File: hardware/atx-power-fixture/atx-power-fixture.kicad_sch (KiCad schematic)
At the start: 32 parts, among them J1 ATX24RH, J2 Screw_Terminal_01x02, J3 BINDING_POST, J4 BINDING_POST, J5 Console FTDI, Q1 DMG2301L, Q2 2N7002, SW1 SW_SPST, SW2 SW_SPST, U1 SSD1306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

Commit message: Layout + gerbers for ATX power fixture
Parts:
- D1: footprint UltraLibrarian:355010RFT -> LED_THT:LED_D3.0mm
- J2: footprint (none) -> TerminalBlock:TerminalBlock_Altech_AK300-2_P5.00mm
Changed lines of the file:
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@@
       (effects (font (size 1.27 1.27)) (justify left))
     )
-    (property "Footprint" "" (id 2) (at 256.159 60.452 0)
+    (property "Footprint" "TerminalBlock:TerminalBlock_Altech_AK300-2_P5.00mm" (id 2) (at 256.159 60.452 0)
       (effects (font (size 1.27 1.27)) hide)
     )
@@
     (property "Reference" "D1" (id 0) (at 116.7765 103.251 0))
     (property "Value" "LED" (id 1) (at 116.7765 105.791 0))
-    (property "Footprint" "UltraLibrarian:355010RFT" (id 2) (at 115.189 110.109 0)
+    (property "Footprint" "LED_THT:LED_D3.0mm" (id 2) (at 115.189 110.109 0)
       (effects (font (size 1.27 1.27)) hide)
     )
@@
     )
     (path "/f43d542b-9e51-43f6-abab-b13ad18f0eab"
-      (reference "D1") (unit 1) (value "LED") (footprint "UltraLibrarian:355010RFT")
+      (reference "D1") (unit 1) (value "LED") (footprint "LED_THT:LED_D3.0mm")
     )
     (path "/5b49dbbc-6d9b-40fe-9cc9-73d9104b1539"

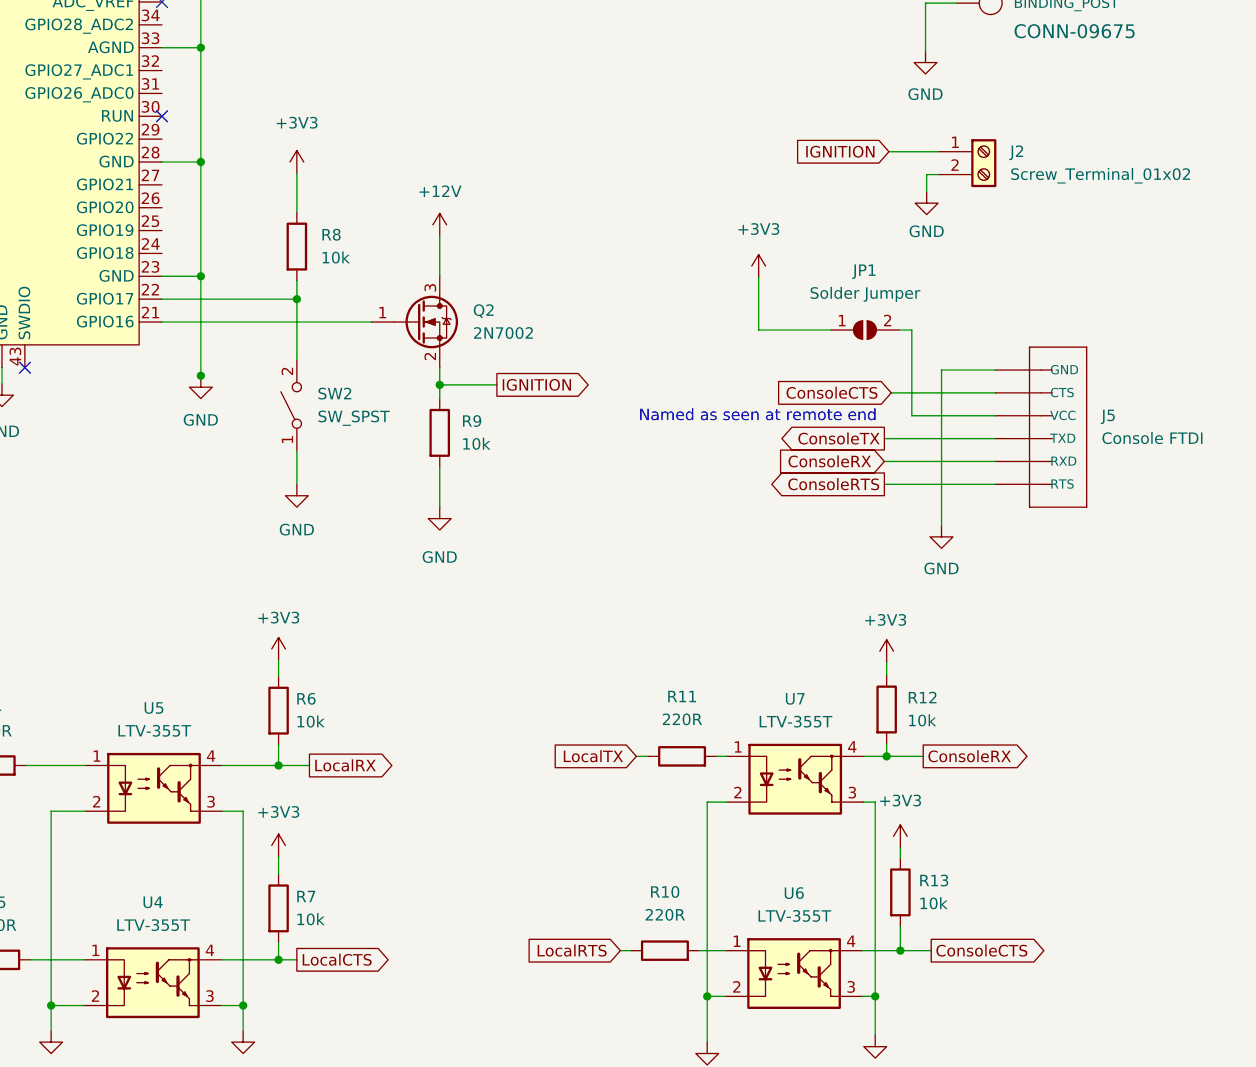
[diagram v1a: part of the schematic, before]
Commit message: Adding first run of firmware for the ATX board
- displays shunt voltage, bus voltage, current, power
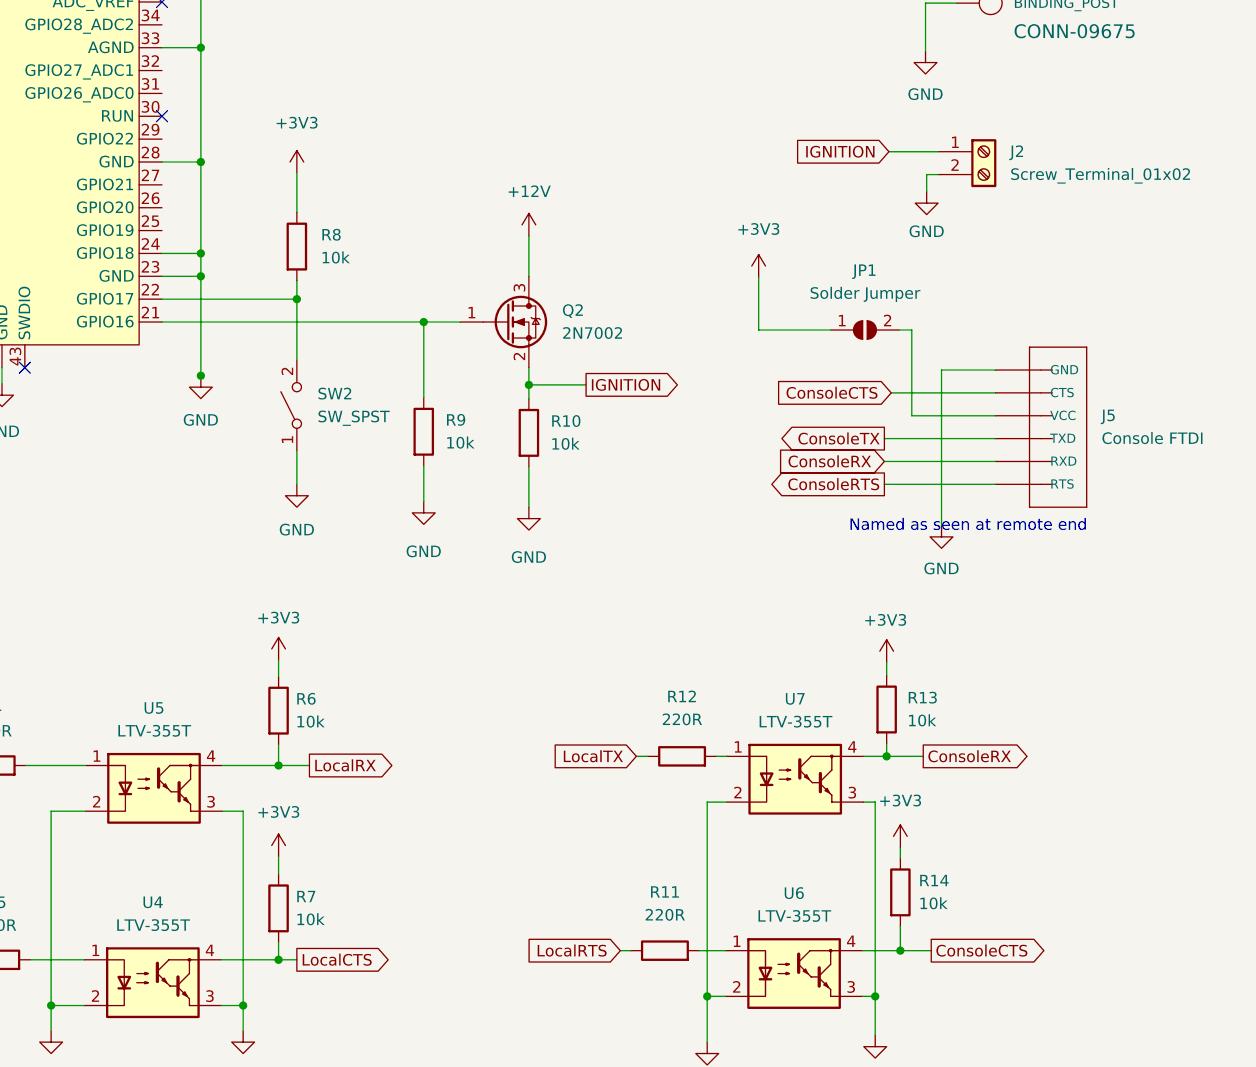
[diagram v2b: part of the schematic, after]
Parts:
- added R9: 10k, Resistor_SMD:R_0805_2012Metric_Pad1.20x1.40mm_HandSolder, symbol Device:R
- renumbered R9 to R10, R10 to R11, R11 to R12, R12 to R13, R13 to R14
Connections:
- net GND: now also U3.24 (GPIO18), R9.2
- net at Q2.1 (G), U3.21 (GPIO16): now also R9.1
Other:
- moved on the sheet: Q2, R10

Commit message: Add title block info, add PDFs
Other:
- company: (none) -> Gavin Hurlbut
- title: (none) -> ATX Power Fixture
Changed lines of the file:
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@@
 (kicad_sch (version 20211123) (generator eeschema)
   (paper "A4")
+  (title_block
+    (title "ATX Power Fixture")
+    (date "2023-01-31")
+    (rev "1.0")
+    (company "Gavin Hurlbut")
+  )
   (junction (at 246.888 149.225) (diameter 0) (color 0 0 0 0)
   )

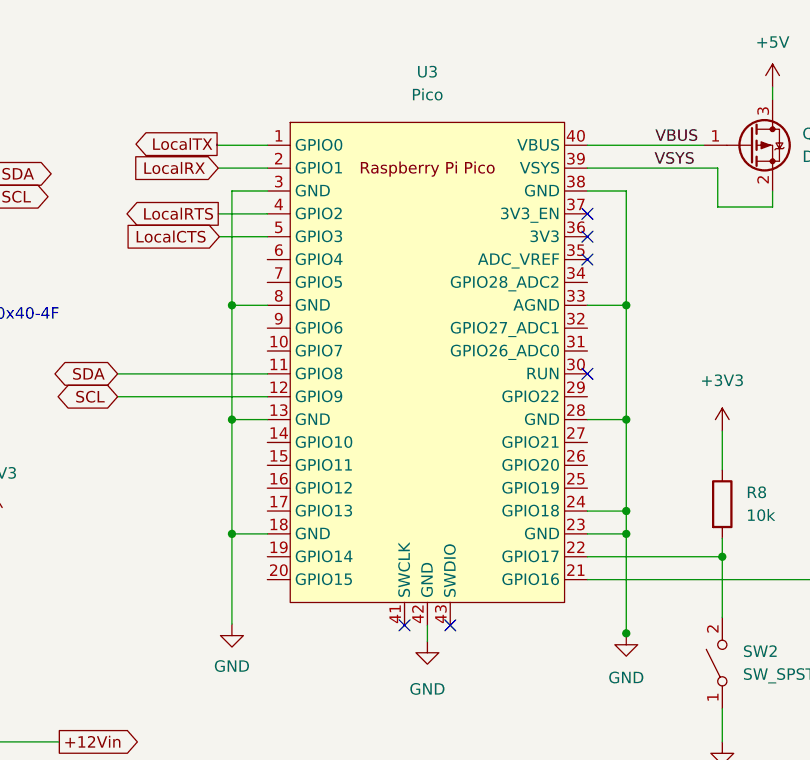
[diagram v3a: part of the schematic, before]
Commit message: Switch the ATX board to use Pico W
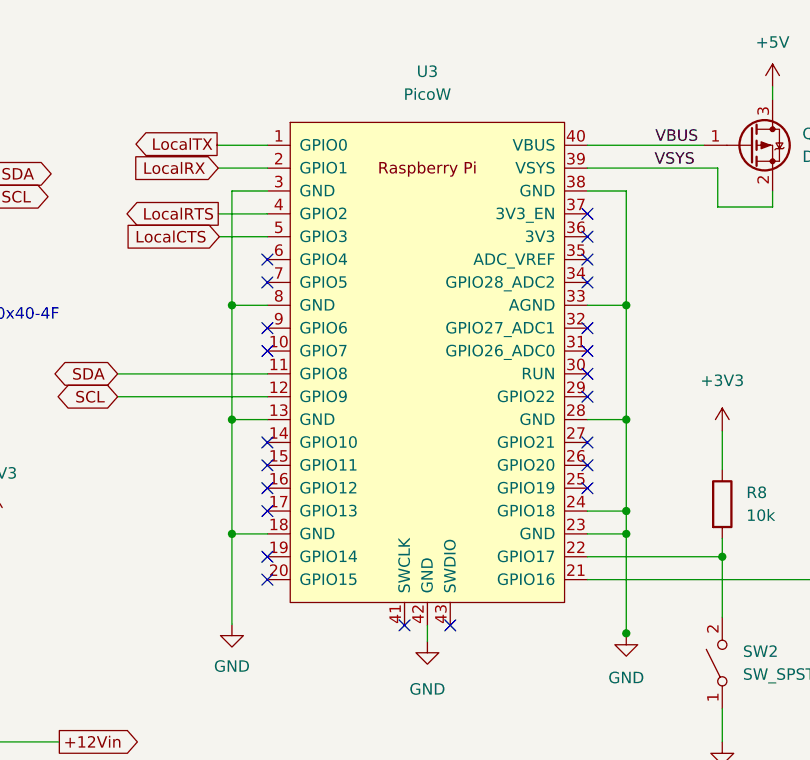
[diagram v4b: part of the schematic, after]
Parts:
- removed U3: Pico, RPi_Pico:RPi_Pico_SMD_TH, symbol MCU_RaspberryPi_and_Boards:Pico
- added U3: PicoW, RPi_Pico:RPi_PicoW_SMD_TH, symbol RPi_Pico:PicoW
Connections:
- net GND: now also U3.13 (GND), U3.18 (GND), U3.23 (GND), U3.24 (GPIO18), U3.28 (GND), U3.3 (GND), U3.33 (AGND), U3.38 (GND), U3.42 (GND), U3.8 (GND)
- net LocalCTS: now also U3.5 (GPIO3)
- net LocalRTS: now also U3.4 (GPIO2)
- net LocalRX: now also U3.2 (GPIO1)
- net LocalTX: now also U3.1 (GPIO0)
- net SCL: now also U3.12 (GPIO9)
- net SDA: now also U3.11 (GPIO8)
- net VBUS: now also U3.40 (VBUS)
- net VSYS: now also U3.39 (VSYS)
- net at R8.2, SW2.2 (B): now also U3.22 (GPIO17)
- net at Q2.1 (G), R9.1: now also U3.21 (GPIO16)
- no-connect marks 9 -> 26

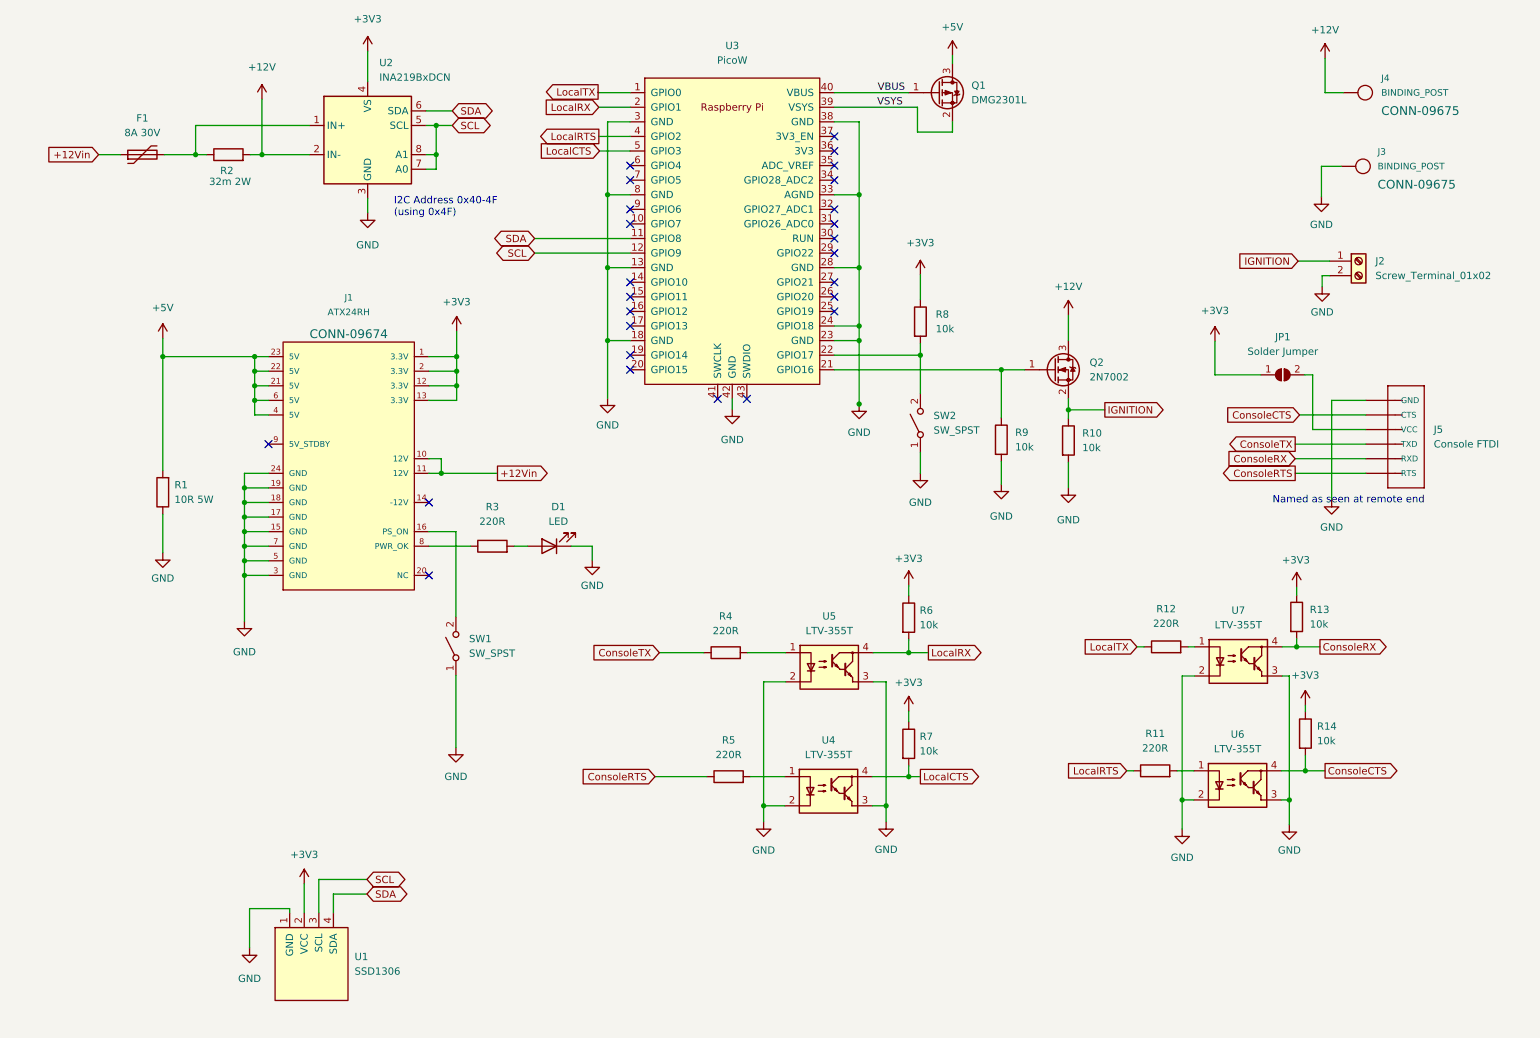
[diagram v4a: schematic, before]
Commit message: Converted atx-power-fixture to PlatformIO, and to STM32F042F6
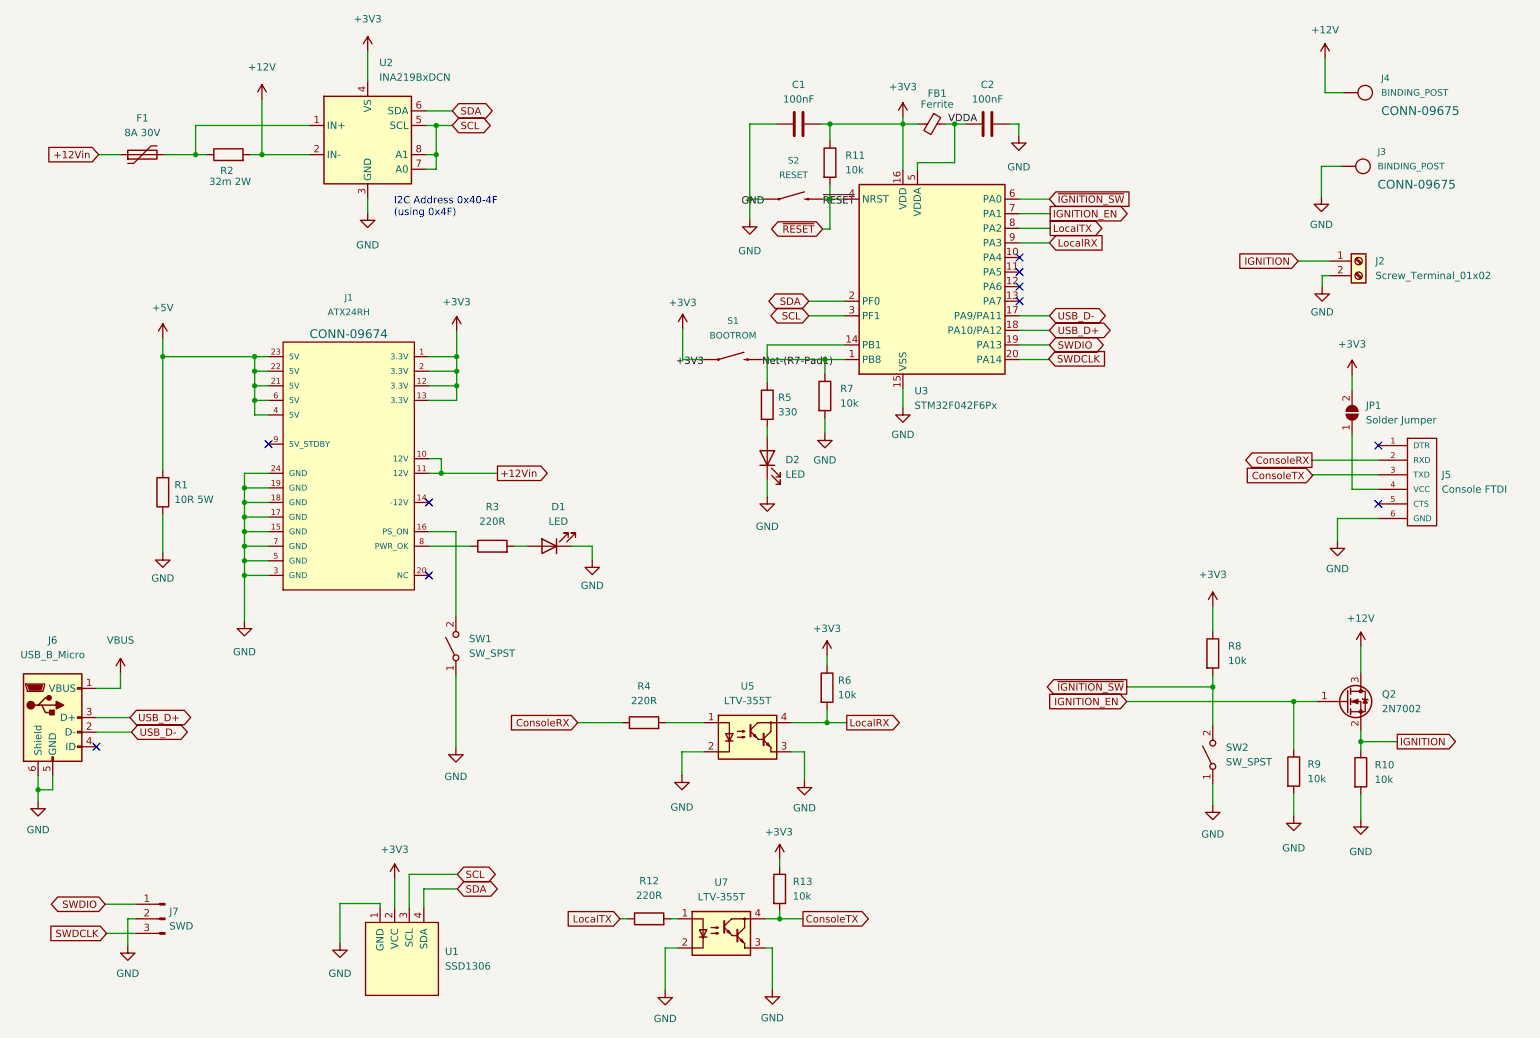
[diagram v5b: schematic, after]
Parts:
- removed Q1: DMG2301L, Package_TO_SOT_SMD:SOT-23, symbol Transistor_FET:DMG2301L
- removed R14: 10k, Resistor_SMD:R_0805_2012Metric_Pad1.20x1.40mm_HandSolder, symbol Device:R
- removed U3: PicoW, RPi_Pico:RPi_PicoW_SMD_TH, symbol RPi_Pico:PicoW
- removed U4, U6: LTV-355T, Package_SO:SO-4_4.4x3.6mm_P2.54mm, symbol Isolator:LTV-355T
- added C1, C2: 100nF, Capacitor_SMD:C_0805_2012Metric_Pad1.18x1.45mm_HandSolder, symbol Device:C
- added D2: LED, LED_SMD:LED_0805_2012Metric_Pad1.15x1.40mm_HandSolder, symbol Device:LED
- added FB1: Ferrite, Inductor_SMD:L_0805_2012Metric_Pad1.15x1.40mm_HandSolder, symbol Device:FerriteBead_Small
- added J6: USB_B_Micro, Connector_USB:USB_Micro-B_Amphenol_10118194_Horizontal, symbol Connector:USB_B_Micro
- added J7: SWD, Connector_PinHeader_2.54mm:PinHeader_1x03_P2.54mm_Vertical, symbol Connector:Conn_01x03_Male
- added S1: BOOTROM, SparkFun-Switches:TACTILE_SWITCH_PTH_6.0MM, symbol Beirdo:MOMENTARY-SWITCH-SPST-PTH-6.0MM
- added S2: RESET, SparkFun-Switches:TACTILE_SWITCH_PTH_6.0MM, symbol Beirdo:MOMENTARY-SWITCH-SPST-PTH-6.0MM
- added U3: STM32F042F6Px, Package_SO:TSSOP-20_4.4x6.5mm_P0.65mm, symbol MCU_ST_STM32F0:STM32F042F6Px
- J2: footprint TerminalBlock:TerminalBlock_Altech_AK300-2_P5.00mm -> TerminalBlock_TE-Connectivity:TerminalBlock_TE_282834-2_1x02_P2.54mm_Horizontal
- J5: footprint Beirdo:FTDI_BASIC -> Beirdo:FTDI-TARGET; symbol Beirdo:FTDI_BASICPTH -> Beirdo:FTDI-TARGET
- R11: value 220R -> 10k
- R5: value 220R -> 330
- U2: symbol Analog_ADC:INA219BxDCN -> Beirdo:INA219BxDCN
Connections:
- net ConsoleCTS is gone; now on net ConsoleRX: J5.2 (RXD)
- net LocalCTS is gone; now on net GND: R7.2
- net LocalRTS is gone; now on net +3V3: R11.1
- net +3V3: now also JP1.2 (B), C1.2, FB1.2, S1.1, S1.2 (1), U3.16 (VDD); no longer JP1.1 (A), R7.1
- net ConsoleRX: now also R4.1; no longer J5.5 (RXD), R13.2, U7.4
- net ConsoleTX: now also J5.3 (TXD), R13.2, U7.4; no longer J5.4 (TXD), R4.1
- net GND: now also J5.6 (GND), C1.1, C2.2, D2.1 (K), J6.5 (GND), J6.6 (Shield), J7.2 (Pin_2), S2.1, S2.2 (1), U3.15 (VSS); no longer J5.1 (GND)
- net LocalRX: now also U3.9 (PA3)
- net LocalTX: now also U3.8 (PA2)
- net SCL: now also U3.3 (PF1)
- net SDA: now also U3.2 (PF0)
- net VBUS: now also J6.1 (VBUS)
- net ~{RESET}: now reaches R11.2
- net ~{RESET}: now also S2.3 (2), S2.4 (2), U3.4 (NRST)
- net at R5.2: now also D2.2 (A)
- net ~{IGNITION_SW}: now reaches R8.2, SW2.2 (B)
- net ~{IGNITION_SW}: now also U3.6 (PA0)
- net IGNITION_EN: now reaches Q2.1 (G), R9.1
- net IGNITION_EN: now also U3.7 (PA1)
- net ConsoleRTS: no longer names the net of R5.1
- net ConsoleRTS: now also U3.14 (PB1); no longer J5.6 (RTS)
- new net: J5.4 (VCC), JP1.1 (A)
- new net: R7.1, S1.3 (2), U3.1 (PB8)
- new net Net-(R7-Pad1): S1.4 (2)
- new net SWDCLK: J7.3 (Pin_3), U3.20 (PA14)
- new net SWDIO: J7.1 (Pin_1), U3.19 (PA13)
- new net USB_D+: J6.3 (D+), U3.18 (PA10/PA12)
- new net USB_D-: J6.2 (D-), U3.17 (PA9/PA11)
- new net VDDA: C2.1, FB1.1, U3.5 (VDDA)
- no-connect marks 26 -> 10
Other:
- note removed: "Named as seen at remote end"
- moved on the sheet: JP1, Q2, R10, R12, R13, R4, R6, R8, R9, SW2, U1, U5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
